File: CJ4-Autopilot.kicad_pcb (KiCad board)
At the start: 2 copper layers, 317.5 x 57.1 mm, 76 parts, among them J1 CRS encoder, J2 FLC encoder, J3 HDG encoder, J4 ALT encoder, J5 CRS encoder, J6 USB_B_Micro, J7 Conn_01x02, SW1 FD1, SW10 ALT, SW11 YD, SW12 XFR, SW13 AP, SW14 FD2, SW15 DISC, SW16 VS encoder, SW2 VS, SW3 VNAV, SW4 FLC, SW5 NAV, SW6 BANK, SW7 HDG, SW8 APPR, SW9 BC, U1 TLC5917IN, U2 AMS1117-3.3, U3 TLC5917IN, U4 74HC165, U5 74HC165, U6 W25Q128JVS, U7 RP2040, Y1 X322512MSB4SI

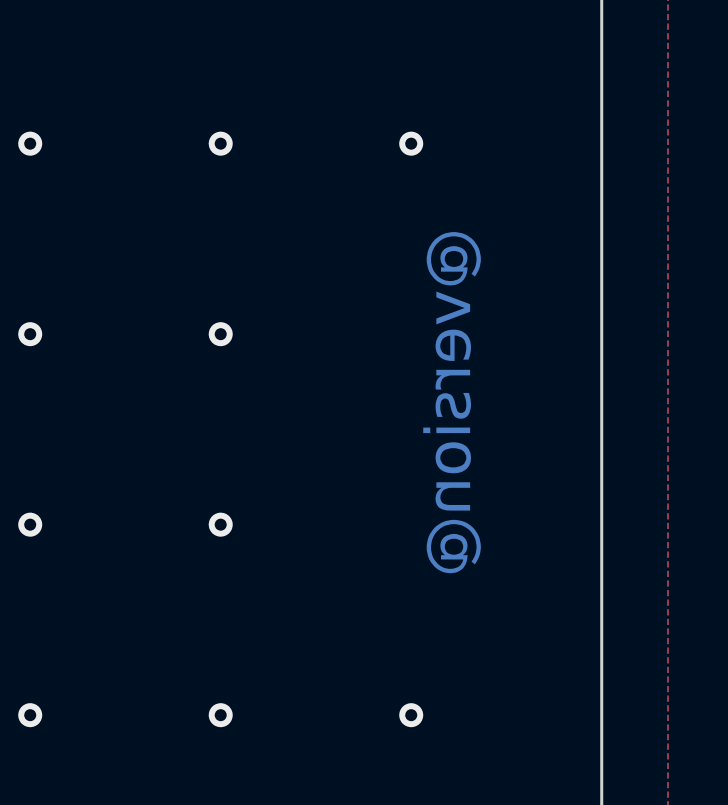
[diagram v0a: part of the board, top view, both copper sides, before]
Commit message: JLCPCB rotation update, add missing pin 1 indicator
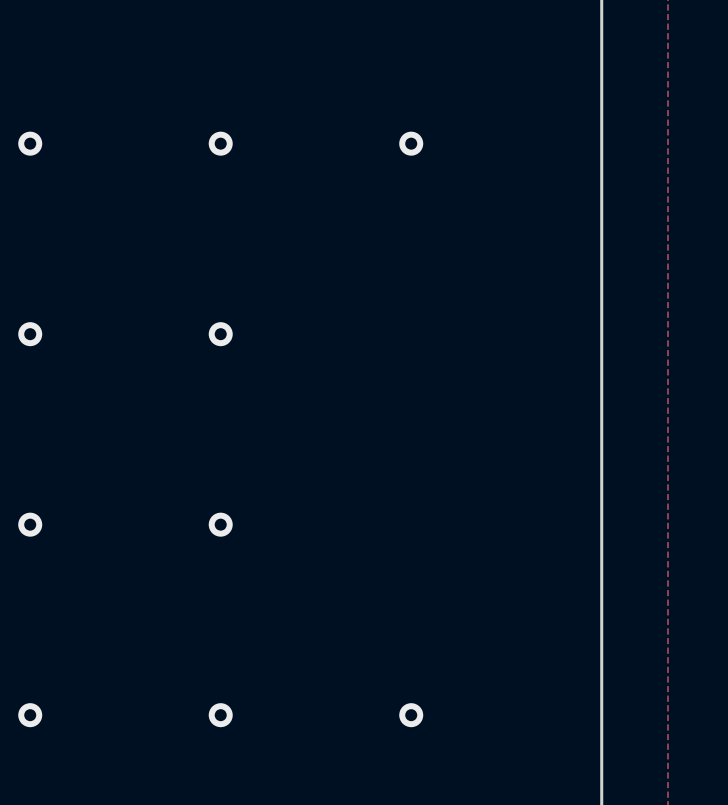
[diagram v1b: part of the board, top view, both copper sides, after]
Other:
- board text added: "CJ4 autopilot panel Neil Enns neile@live.com 2022-08-30"
- board text removed: "@version@"
- board text removed: "CJ4 autopilot panel Neil Enns neile@live.com @date@ @version@"
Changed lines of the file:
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@@
   (gr_circle (center 134.72521 68.326) (end 134.47121 68.58) (layer "B.SilkS") (width 0.15) (fill none))
   (gr_circle (center 253.746 80.518) (end 253.492 80.772) (layer "B.SilkS") (width 0.15) (fill none))
+  (gr_circle (center 143.764 61.468) (end 143.51 61.722) (layer "B.SilkS") (width 0.15) (fill none))
+  (gr_circle (center 168.91 77.216) (end 168.656 77.47) (layer "B.SilkS") (width 0.15) (fill none))
   (gr_circle (center 196.85 71.12) (end 196.596 71.374) (layer "B.SilkS") (width 0.15) (fill none))
   (gr_circle (center 303.17079 71.628) (end 302.91679 71.882) (layer "B.SilkS") (width 0.15) (fill none))
@@
   (gr_line (start 21.59 43.18) (end 334.01 43.18) (layer "Edge.Cuts") (width 0.1))
   (gr_arc (start 84.6582 55.609) (mid 85.104569 54.531369) (end 86.1822 54.085) (layer "Edge.Cuts") (width 0.1))
-  (gr_text "@version@" (at 331.47 70.866 90) (layer "B.Cu")
+  (gr_text "" (at 331.47 70.866 90) (layer "B.Cu")
     (effects (font (size 1.5 1.5) (thickness 0.3)) (justify mirror))
   )
@@
     (effects (font (size 1 1) (thickness 0.15)) (justify mirror))
   )
-  (gr_text "CJ4 autopilot panel\nNeil Enns neile@live.com\n@date@\n@version@" (at 273.812 94.234) (layer "B.SilkS")
+  (gr_text "CJ4 autopilot panel\nNeil Enns neile@live.com\n2022-08-30\n" (at 273.812 94.234) (layer "B.SilkS")
     (effects (font (size 1 1) (thickness 0.15)) (justify mirror))
   )

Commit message: Fix broken version text, add more vias
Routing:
- net HDG_BTN: track 55.7 -> 56.4 mm
- net ALT_A: track 103.6 -> 104.2 mm
- net ALT_B: track 108.1 -> 108.6 mm
- net GND: vias 185 -> 244
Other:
- board text added: "@version@"
- board text added: "CJ4 autopilot panel Neil Enns neile@live.com 2022-08-30 @version@"
- board text removed: "CJ4 autopilot panel Neil Enns neile@live.com 2022-08-30"

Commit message: Add missing net labels
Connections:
- net Net-(R6-Pad2) renamed /RP2040/USB_D+R
- net Net-(R7-Pad2) renamed /RP2040/USB_D-R
- R1 pad 1: Net-(R1-Pad1) -> /REXT
- R2 pad 1: Net-(R2-Pad1) -> /REXT
- U1 pad 15: Net-(R1-Pad1) -> /REXT
- U3 pad 15: Net-(R2-Pad1) -> /REXT
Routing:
- net /REXT: track 0.00 -> 3.90 mm
- net Net-(R1-Pad1): track 1.95 -> 0.00 mm
- net Net-(R2-Pad1): track 1.95 -> 0.00 mm
